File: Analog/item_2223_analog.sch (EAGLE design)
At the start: 74 parts, among them IC1 MCP1525TO, IC2 MCP6004SO, IC4 MCP6004SO, IC5 MCP6004SO, IC6 MCP3204SL, IC7 LM336LP

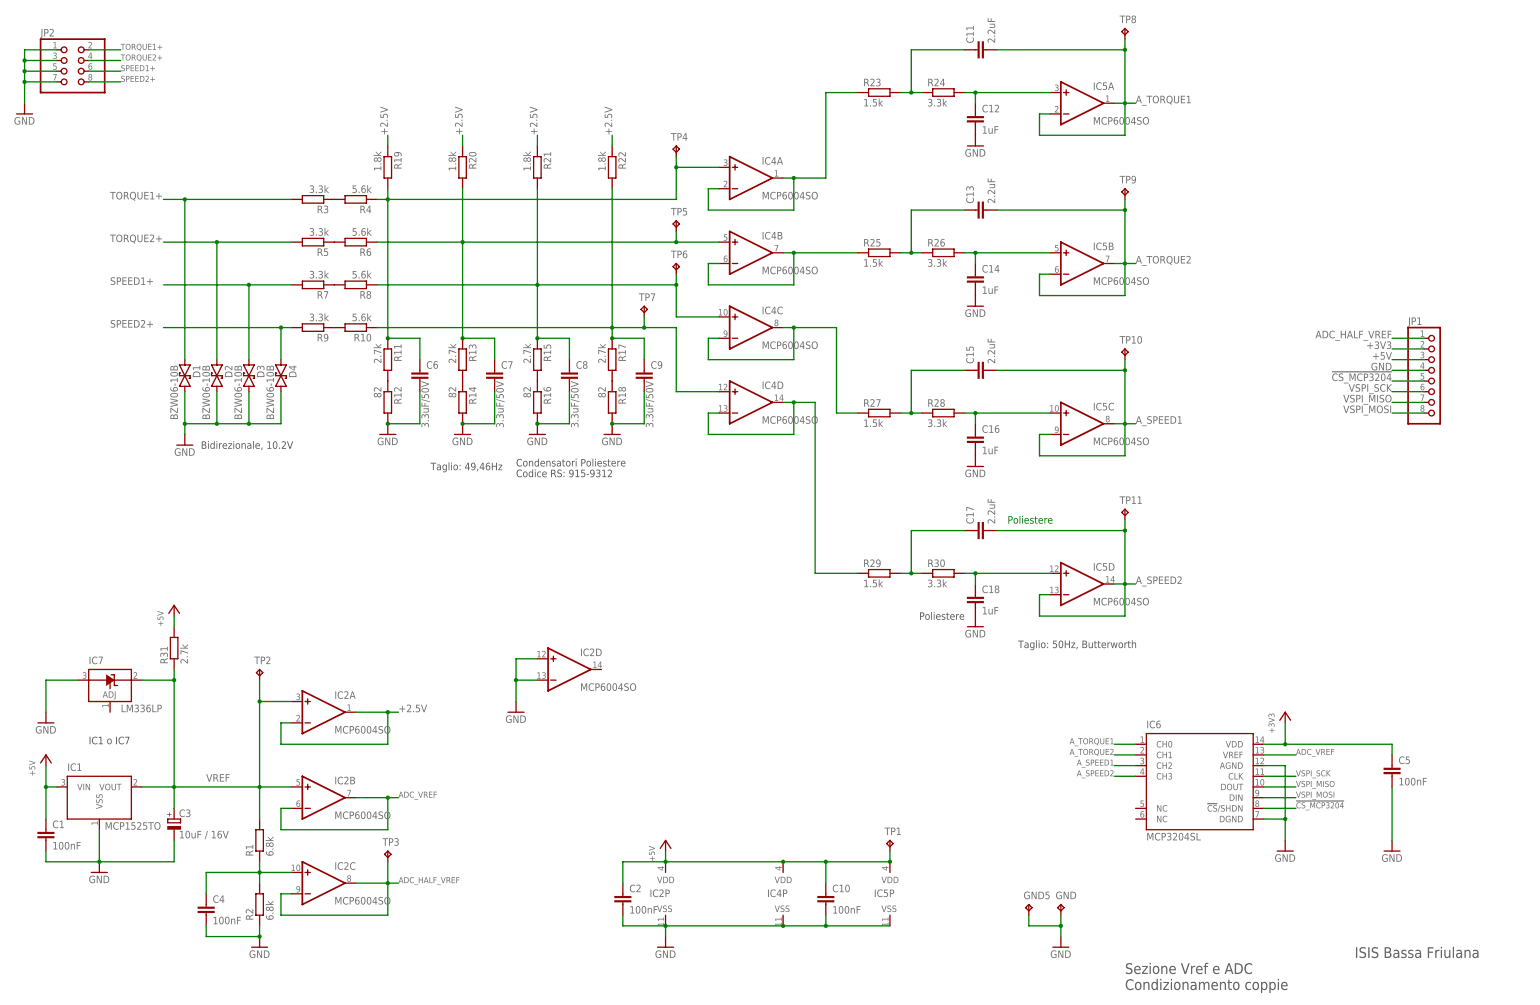
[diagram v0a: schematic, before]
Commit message: ingresso differenziale e AGND
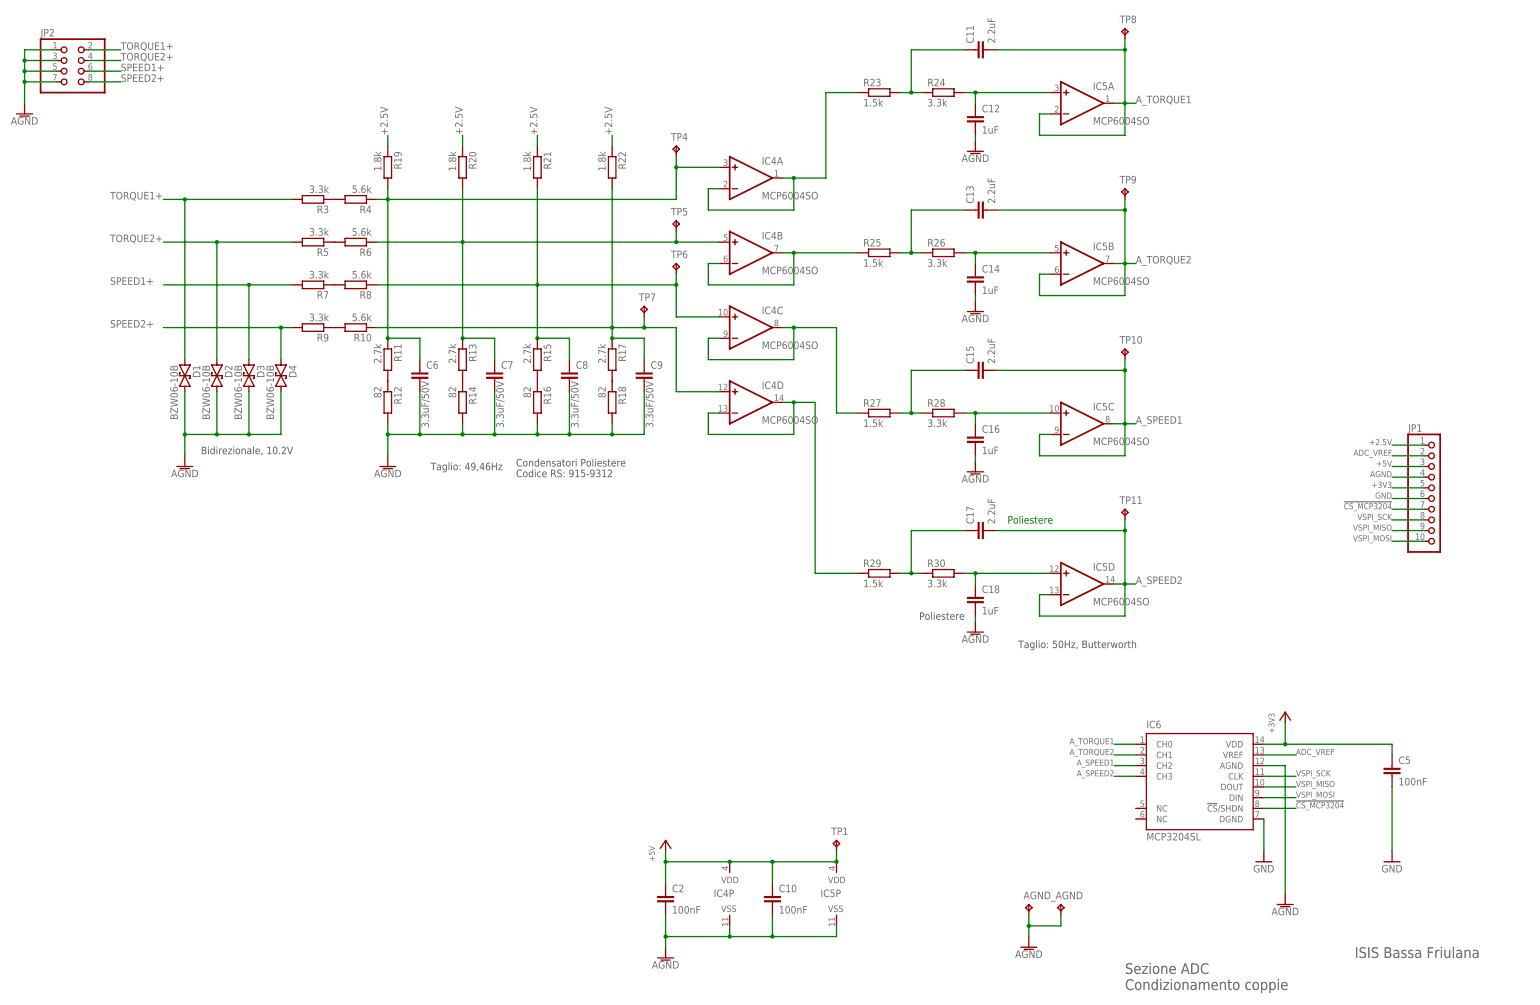
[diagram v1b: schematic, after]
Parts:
- removed C1, C4: 100nF, rcl_LargePads:C-EUC0805
- removed C3: 10uF / 16V, rcl_LargePads:CPOL-EUC
- removed IC1: MCP1525TO, MCP1525_MCP1541:MCP1525TO
- removed IC2: MCP6004SO, MCP6002_MCP6004:MCP6004SO
- removed IC7: LM336LP, linear:LM336LP
- removed R1, R2: 6.8k, rcl_LargePads:R-EU_R0805
- removed R31: 2.7k, rcl:R-EU_R0805
- removed TP2, TP3: TPTP16R, testpad:TPTP16R
- JP1: device pinhead:PINHD-1X8 -> pinhead:PINHD-1X10
- renumbered GND to AGND, GND5 to AGND_
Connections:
- removed net ADC_HALF_VREF: IC2C.-IN, IC2C.OUT, JP1.1, TP3.TP
- removed net N$3: C4.1, IC2C.+IN, R1.1, R2.2
- removed net VREF: C3.+, IC1.VOUT, IC2A.+IN, IC2B.+IN, IC7.C, R1.2, R31.1, TP2.TP
- new net AGND: AGND.TP, AGND_.TP, C10.2, C12.2, C14.2, C16.2, C18.2, C2.2, C6.2, C7.2, C8.2, C9.2, D1.2, D2.2, D3.2, D4.2, IC4P.VSS, IC5P.VSS, IC6.AGND, JP1.4, JP2.1, JP2.3, JP2.5, JP2.7, R12.2, R14.2, R16.2, R18.2
- net !CS_MCP3204!: now also JP1.7; no longer JP1.5
- net +2.5V: now also JP1.1; no longer IC2A.-IN, IC2A.OUT
- net +3V3: now also JP1.5; no longer JP1.2
- net +5V: no longer C1.1, IC1.VIN, IC2P.VDD, R31.2
- net ADC_VREF: now also JP1.2; no longer IC2B.-IN, IC2B.OUT
- net GND: now also JP1.6; no longer AGND.TP, AGND_.TP, C1.2, C10.2, C12.2, C14.2, C16.2, C18.2, C2.2, C3.-, C4.2, C6.2, C7.2, C8.2, C9.2, D1.2, D2.2, D3.2, D4.2, IC1.VSS, IC2D.+IN, IC2D.-IN, IC2P.VSS, IC4P.VSS, IC5P.VSS, IC6.AGND, IC7.A, JP1.4, JP2.1, JP2.3, JP2.5, JP2.7, R12.2, R14.2, R16.2, R18.2, R2.1
- net VSPI_MISO: now also JP1.9; no longer JP1.7
- net VSPI_MOSI: now also JP1.10; no longer JP1.8
- net VSPI_SCK: now also JP1.8; no longer JP1.6
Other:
- note added: "Sezione ADC Condizionamento coppie"
- note removed: "IC1 o IC7"
- note removed: "Sezione Vref e ADC Condizionamento coppie"
- moved on the sheet: C10, C2, IC4P, IC5P, TP1
